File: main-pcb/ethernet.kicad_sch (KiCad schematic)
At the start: 85 parts, among them J6 0826-1G1T-23-F, Q1 SSM6N58NU, U1 XC7S100-1FGGA484C, U17 S27KS0642GABHI030, U18 ECS-1612MV-250-CN, U20 KSZ9031RN, U21 RCLAMP0514M, U22 RCLAMP0514M, U24 IS25WP256D-JLLE

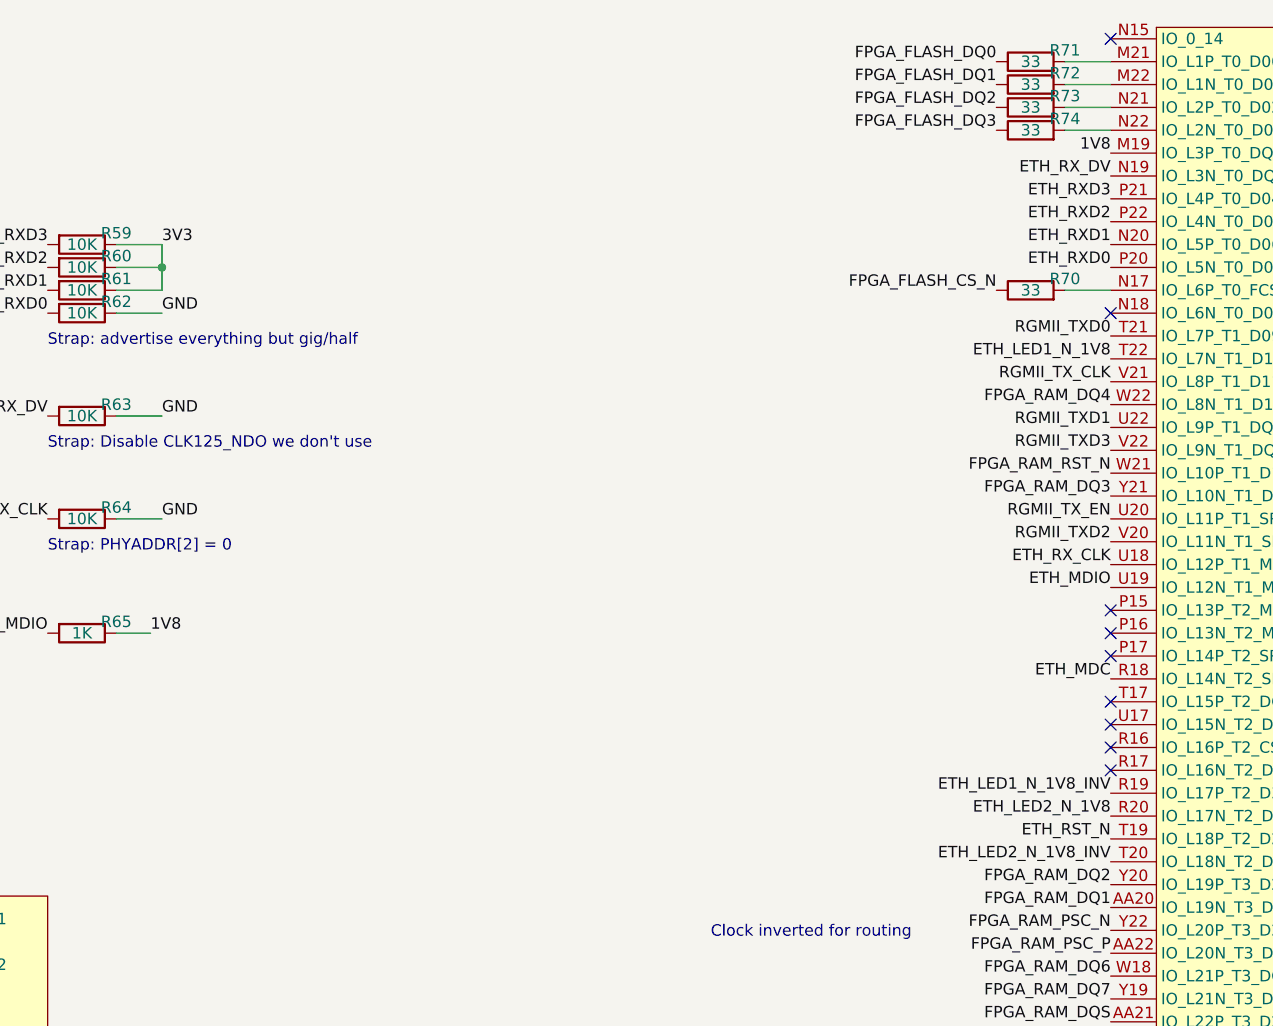
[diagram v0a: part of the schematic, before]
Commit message: Continued routing RGMII PHY
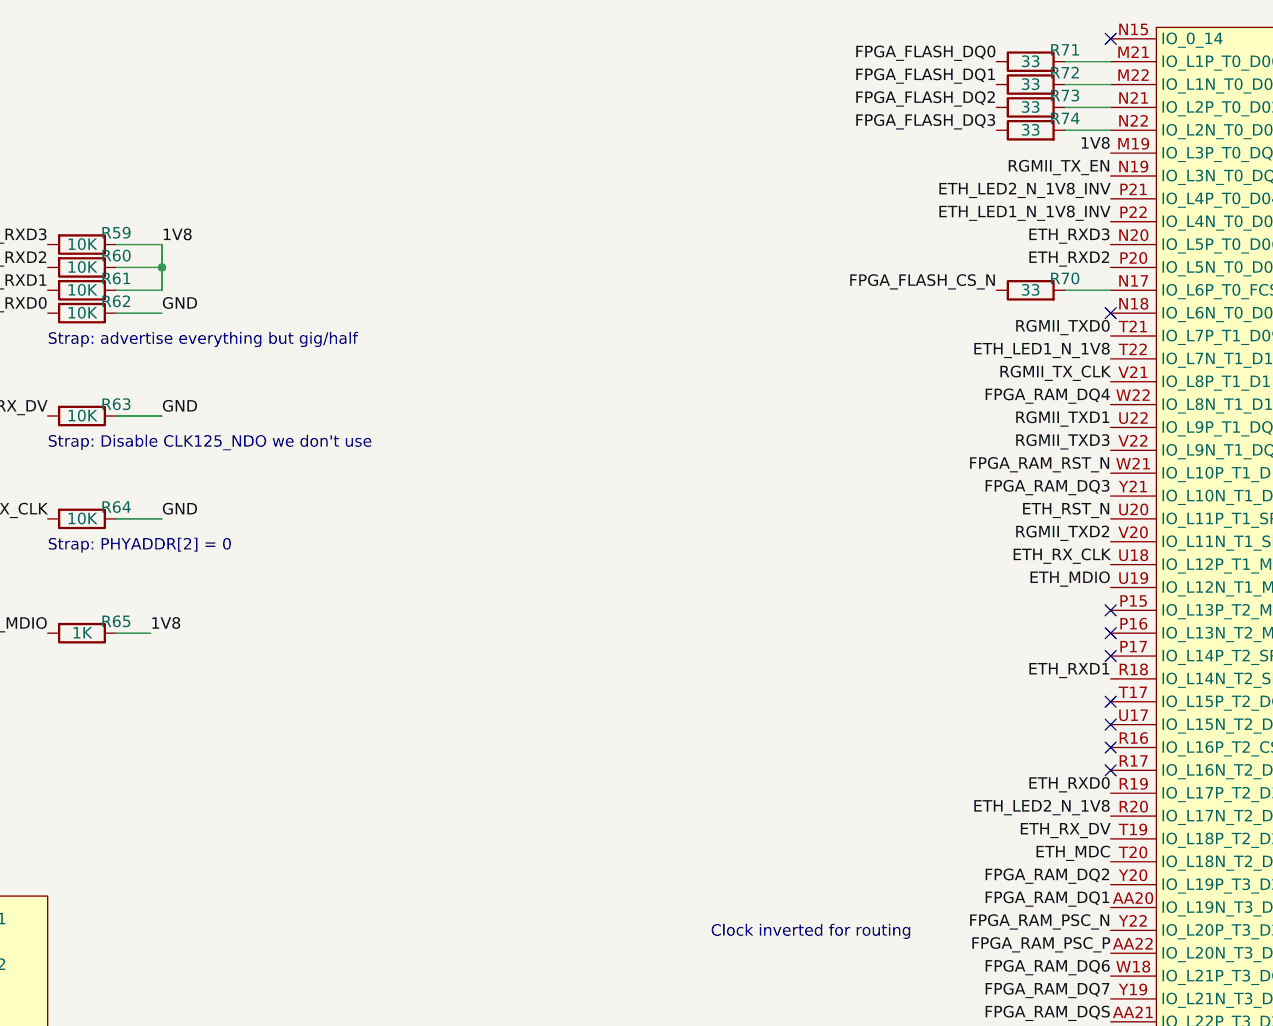
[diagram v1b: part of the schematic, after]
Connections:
- net 1V8: now also R59.1, R60.1, R61.1
- net 3V3: no longer R59.1, R60.1, R61.1
- net ETH_LED1_N_1V8_INV: now also U1.P22 (IO_L4N_T0_D05_14); no longer U1.R19 (IO_L17P_T2_D30_14)
- net ETH_LED2_N_1V8_INV: now also U1.P21 (IO_L4P_T0_D04_14); no longer U1.T20 (IO_L18N_T2_D27_14)
- net ETH_MDC: now also U1.T20 (IO_L18N_T2_D27_14); no longer U1.R18 (IO_L14N_T2_SRCC_14)
- net ETH_RST_N: now also U1.U20 (IO_L11P_T1_SRCC_14); no longer U1.T19 (IO_L18P_T2_D28_14)
- net ETH_RXD0: now also U1.R19 (IO_L17P_T2_D30_14); no longer U1.P20 (IO_L5N_T0_D07_14)
- net ETH_RXD1: now also U1.R18 (IO_L14N_T2_SRCC_14); no longer U1.N20 (IO_L5P_T0_D06_14)
- net ETH_RXD2: now also U1.P20 (IO_L5N_T0_D07_14); no longer U1.P22 (IO_L4N_T0_D05_14)
- net ETH_RXD3: now also U1.N20 (IO_L5P_T0_D06_14); no longer U1.P21 (IO_L4P_T0_D04_14)
- net ETH_RX_DV: now also U1.T19 (IO_L18P_T2_D28_14); no longer U1.N19 (IO_L3N_T0_DQS_EMCCLK_14)
- net RGMII_TX_EN: now also U1.N19 (IO_L3N_T0_DQS_EMCCLK_14); no longer U1.U20 (IO_L11P_T1_SRCC_14)
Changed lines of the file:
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@@
 	)
 	(label "ETH_RX_DV"
-		(at 340.36 38.1 180)
+		(at 340.36 111.76 180)
 		(fields_autoplaced yes)
 		(effects
@@
 	)
 	(label "ETH_RXD2"
-		(at 340.36 43.18 180)
+		(at 340.36 48.26 180)
 		(fields_autoplaced yes)
 		(effects
@@
 	)
 	(label "ETH_RST_N"
-		(at 340.36 111.76 180)
+		(at 340.36 76.2 180)
 		(fields_autoplaced yes)
 		(effects
@@
 	)
 	(label "ETH_LED2_N_1V8_INV"
-		(at 340.36 114.3 180)
+		(at 340.36 40.64 180)
 		(fields_autoplaced yes)
 		(effects
@@
 	)
 	(label "ETH_RXD1"
-		(at 340.36 45.72 180)
+		(at 340.36 93.98 180)
 		(fields_autoplaced yes)
 		(effects
@@
 	)
 	(label "ETH_RXD3"
-		(at 340.36 40.64 180)
+		(at 340.36 45.72 180)
 		(fields_autoplaced yes)
 		(effects
@@
 	)
 	(label "ETH_LED1_N_1V8_INV"
+		(at 340.36 43.18 180)
+		(fields_autoplaced yes)
+		(effects
+			(font
+				(size 1.27 1.27)
+			)
+			(justify right bottom)
+		)
+	)
+	(label "GND"
+		(at 234.95 53.34 0)
+		(fields_autoplaced yes)
+		(effects
+			(font
+				(size 1.27 1.27)
+			)
+			(justify left bottom)
+		)
+	)
+	(label "ETH_RXD0"
 		(at 340.36 106.68 180)
-		(fields_autoplaced yes)
-		(effects
-			(font
-				(size 1.27 1.27)
-			)
-			(justify right bottom)
-		)
-	)
-	(label "GND"
-		(at 234.95 53.34 0)
-		(fields_autoplaced yes)
-		(effects
-			(font
-				(size 1.27 1.27)
-			)
-			(justify left bottom)
-		)
-	)
-	(label "ETH_RXD0"
-		(at 340.36 48.26 180)
 		(fields_autoplaced yes)
 		(effects
@@
 	)
 	(label "ETH_MDC"
-		(at 340.36 93.98 180)
+		(at 340.36 114.3 180)
 		(fields_autoplaced yes)
 		(effects
@@
 	)
 	(label "RGMII_TX_EN"
-		(at 340.36 76.2 180)
+		(at 340.36 38.1 180)
 		(fields_autoplaced yes)
 		(effects
@@
 		)
 	)
-	(label "3V3"
+	(label "1V8"
 		(at 234.95 45.72 0)
 		(fields_autoplaced yes)

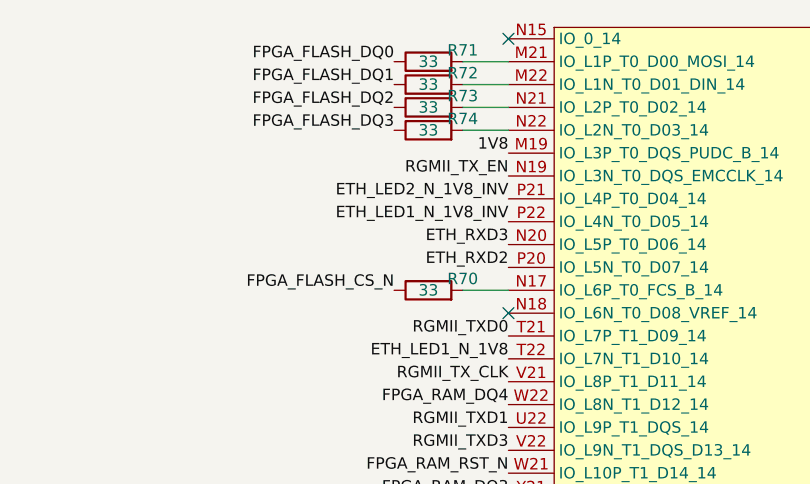
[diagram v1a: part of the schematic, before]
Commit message: Almost fully routed MCU
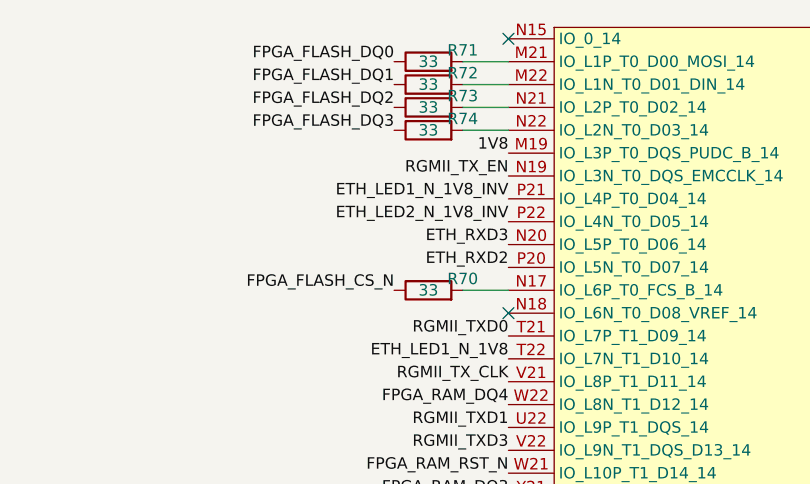
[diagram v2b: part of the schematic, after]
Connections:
- net ETH_LED1_N_1V8_INV: now also U1.P21 (IO_L4P_T0_D04_14); no longer U1.P22 (IO_L4N_T0_D05_14)
- net ETH_LED2_N_1V8_INV: now also U1.P22 (IO_L4N_T0_D05_14); no longer U1.P21 (IO_L4P_T0_D04_14)
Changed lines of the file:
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@@
 	)
 	(label "ETH_LED2_N_1V8_INV"
-		(at 340.36 40.64 180)
+		(at 340.36 43.18 180)
 		(fields_autoplaced yes)
 		(effects
@@
 	)
 	(label "ETH_LED1_N_1V8_INV"
-		(at 340.36 43.18 180)
+		(at 340.36 40.64 180)
 		(fields_autoplaced yes)
 		(effects

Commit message: Began layout of power supply
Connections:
- net ETH_RXD0: now also U1.T19 (IO_L18P_T2_D28_14); no longer U1.R19 (IO_L17P_T2_D30_14)
- net ETH_RX_DV: now also U1.R19 (IO_L17P_T2_D30_14); no longer U1.T19 (IO_L18P_T2_D28_14)
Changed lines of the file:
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@@
 	)
 	(label "ETH_RX_DV"
-		(at 340.36 111.76 180)
+		(at 340.36 106.68 180)
 		(fields_autoplaced yes)
 		(effects
@@
 	)
 	(label "ETH_RXD0"
-		(at 340.36 106.68 180)
-		(fields_autoplaced yes)
-		(effects
+		(at 340.36 111.76 180)
+		(fields_autoplaced yes)
+		(effects
